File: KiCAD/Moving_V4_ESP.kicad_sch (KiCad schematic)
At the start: 59 parts, among them J1 Vin_1, J2 Vin_2, J3 Power_SW, J4 USB_B_Micro, J5 MOTOR_R, J6 Motor_L, Q1 U4_ALT2, Q2 U4_ALT2, Q3 U4_ALT2, SW1 SW_Reset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

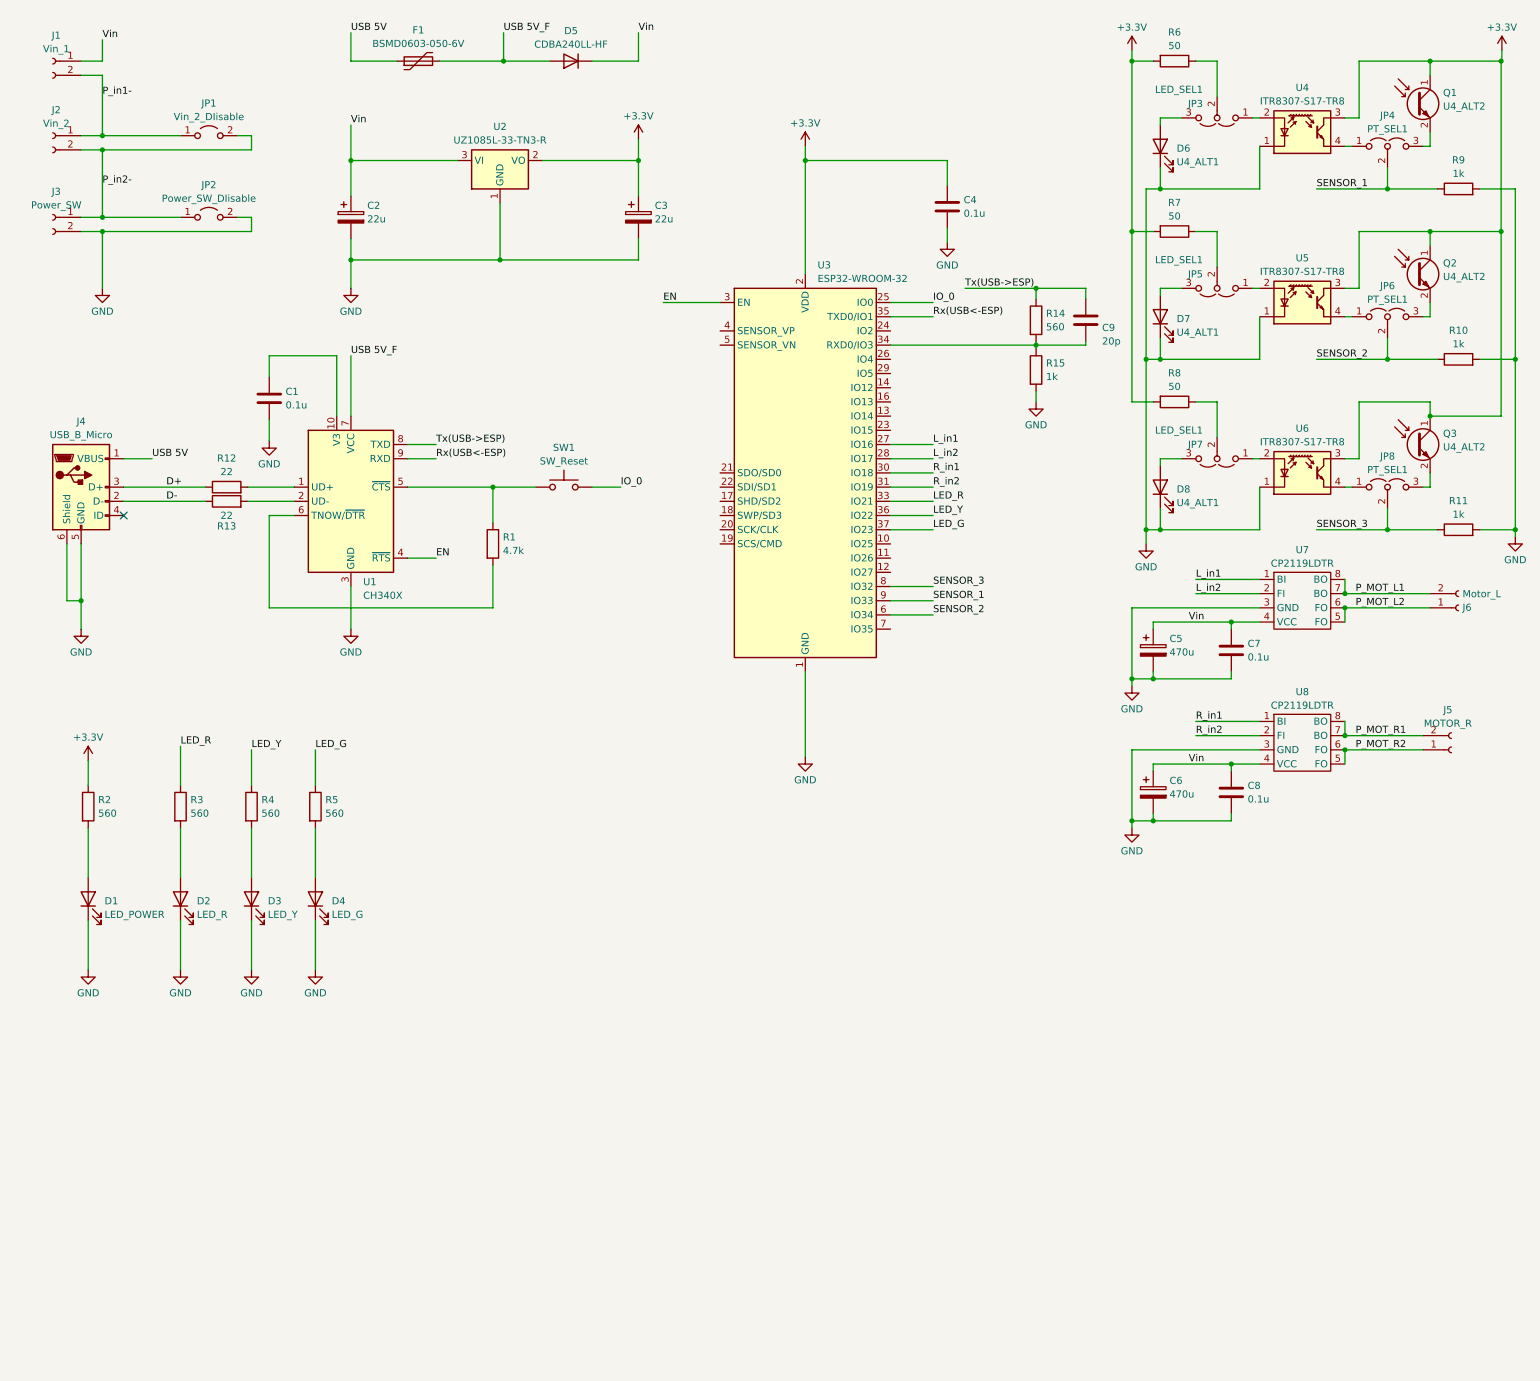
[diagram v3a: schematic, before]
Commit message: 機能ピンのプルアップ・プルダウンを追加
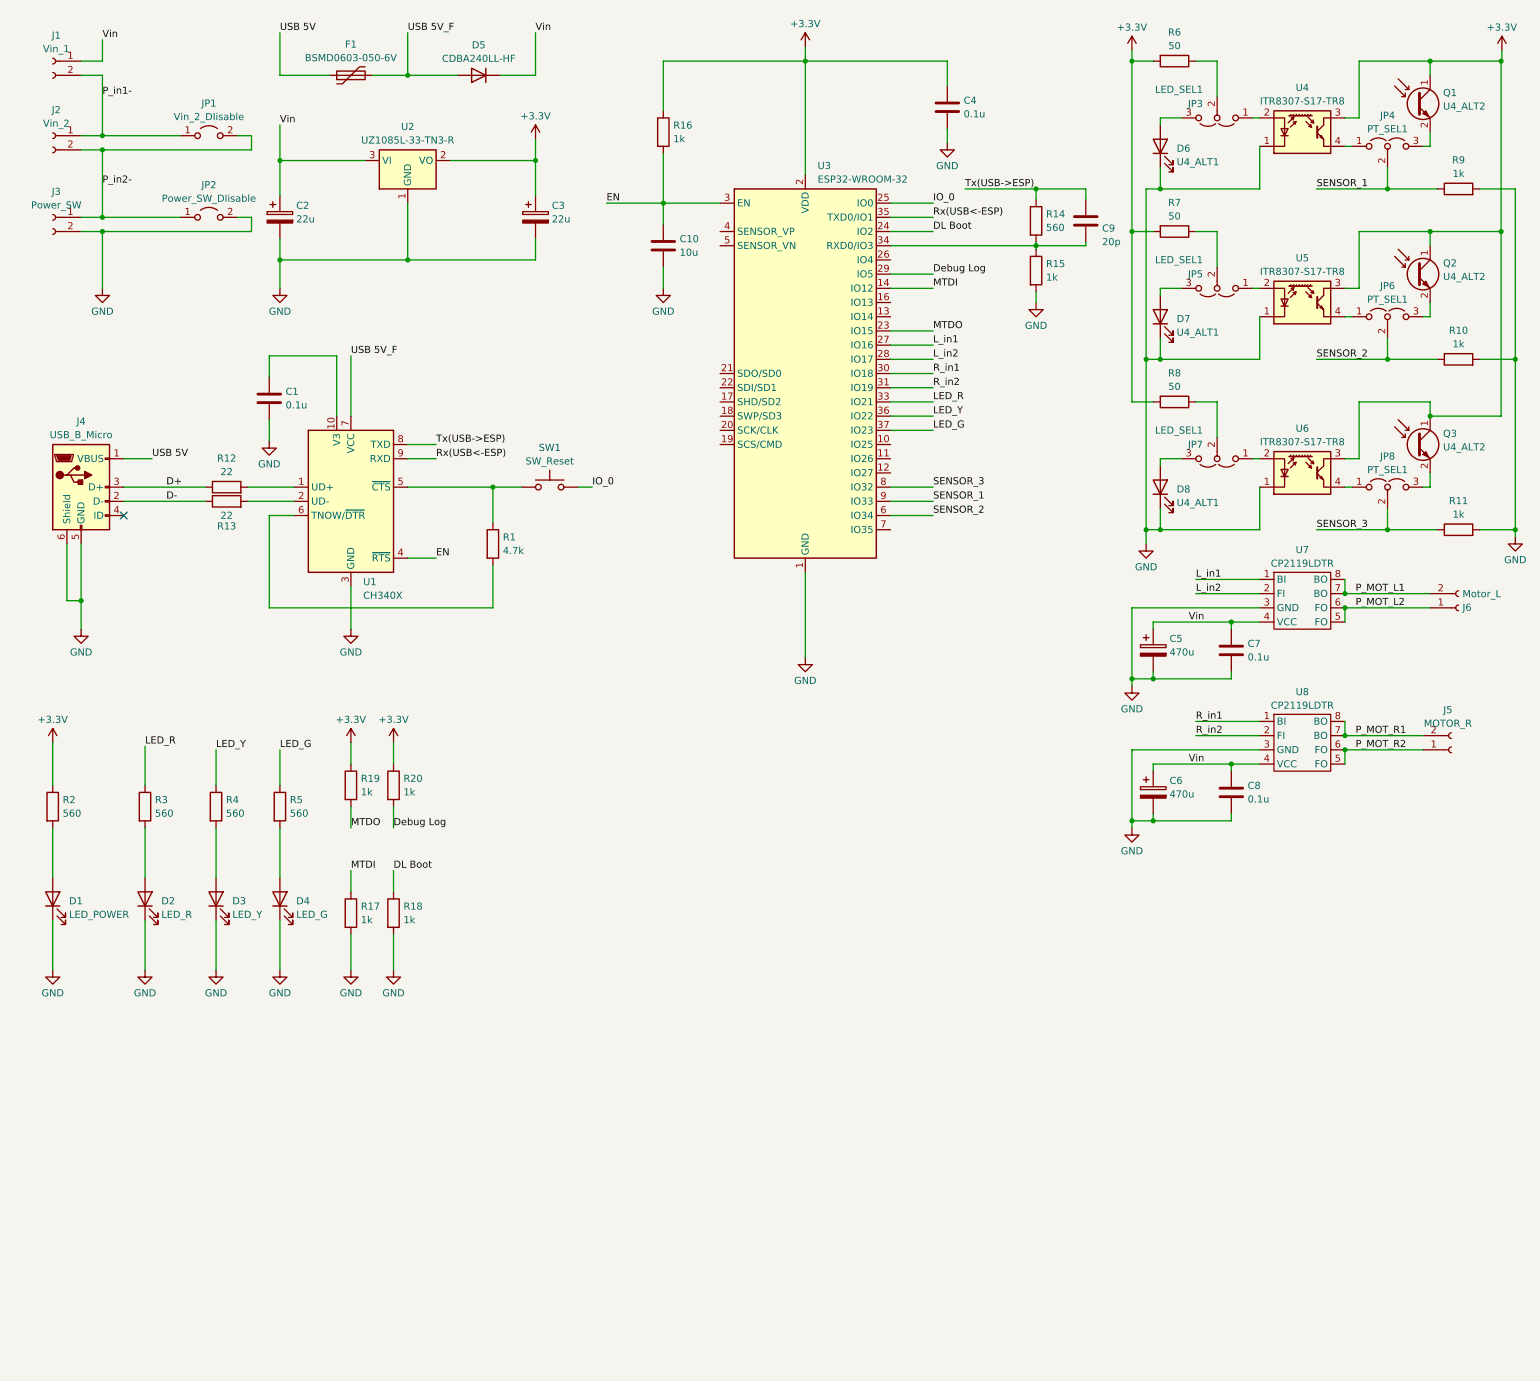
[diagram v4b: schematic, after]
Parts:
- added C10: 10u, Capacitor_SMD:C_0402_1005Metric, symbol Device:C
- added R16, R17, R18, R19, R20: 1k, Resistor_SMD:R_0402_1005Metric, symbol Device:R
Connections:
- net +3.3V: now also R16.1, R19.1, R20.1
- net EN: now also C10.1, R16.2
- net GND: now also C10.2, R17.2, R18.2
- net MTDI: now reaches U3.14 (IO12)
- net MTDI: now also R17.1
- net MTDO: now reaches U3.23 (IO15)
- net MTDO: now also R19.2
- net DL Boot: now reaches U3.24 (IO2)
- net DL Boot: now also R18.1
- net Debug Log: now reaches U3.29 (IO5)
- net Debug Log: now also R20.2
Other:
- moved on the sheet: C2, C3, C4, C9, D1, D2, D3, D4, D5, F1, R14, R15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

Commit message: 5Vの系列を追加
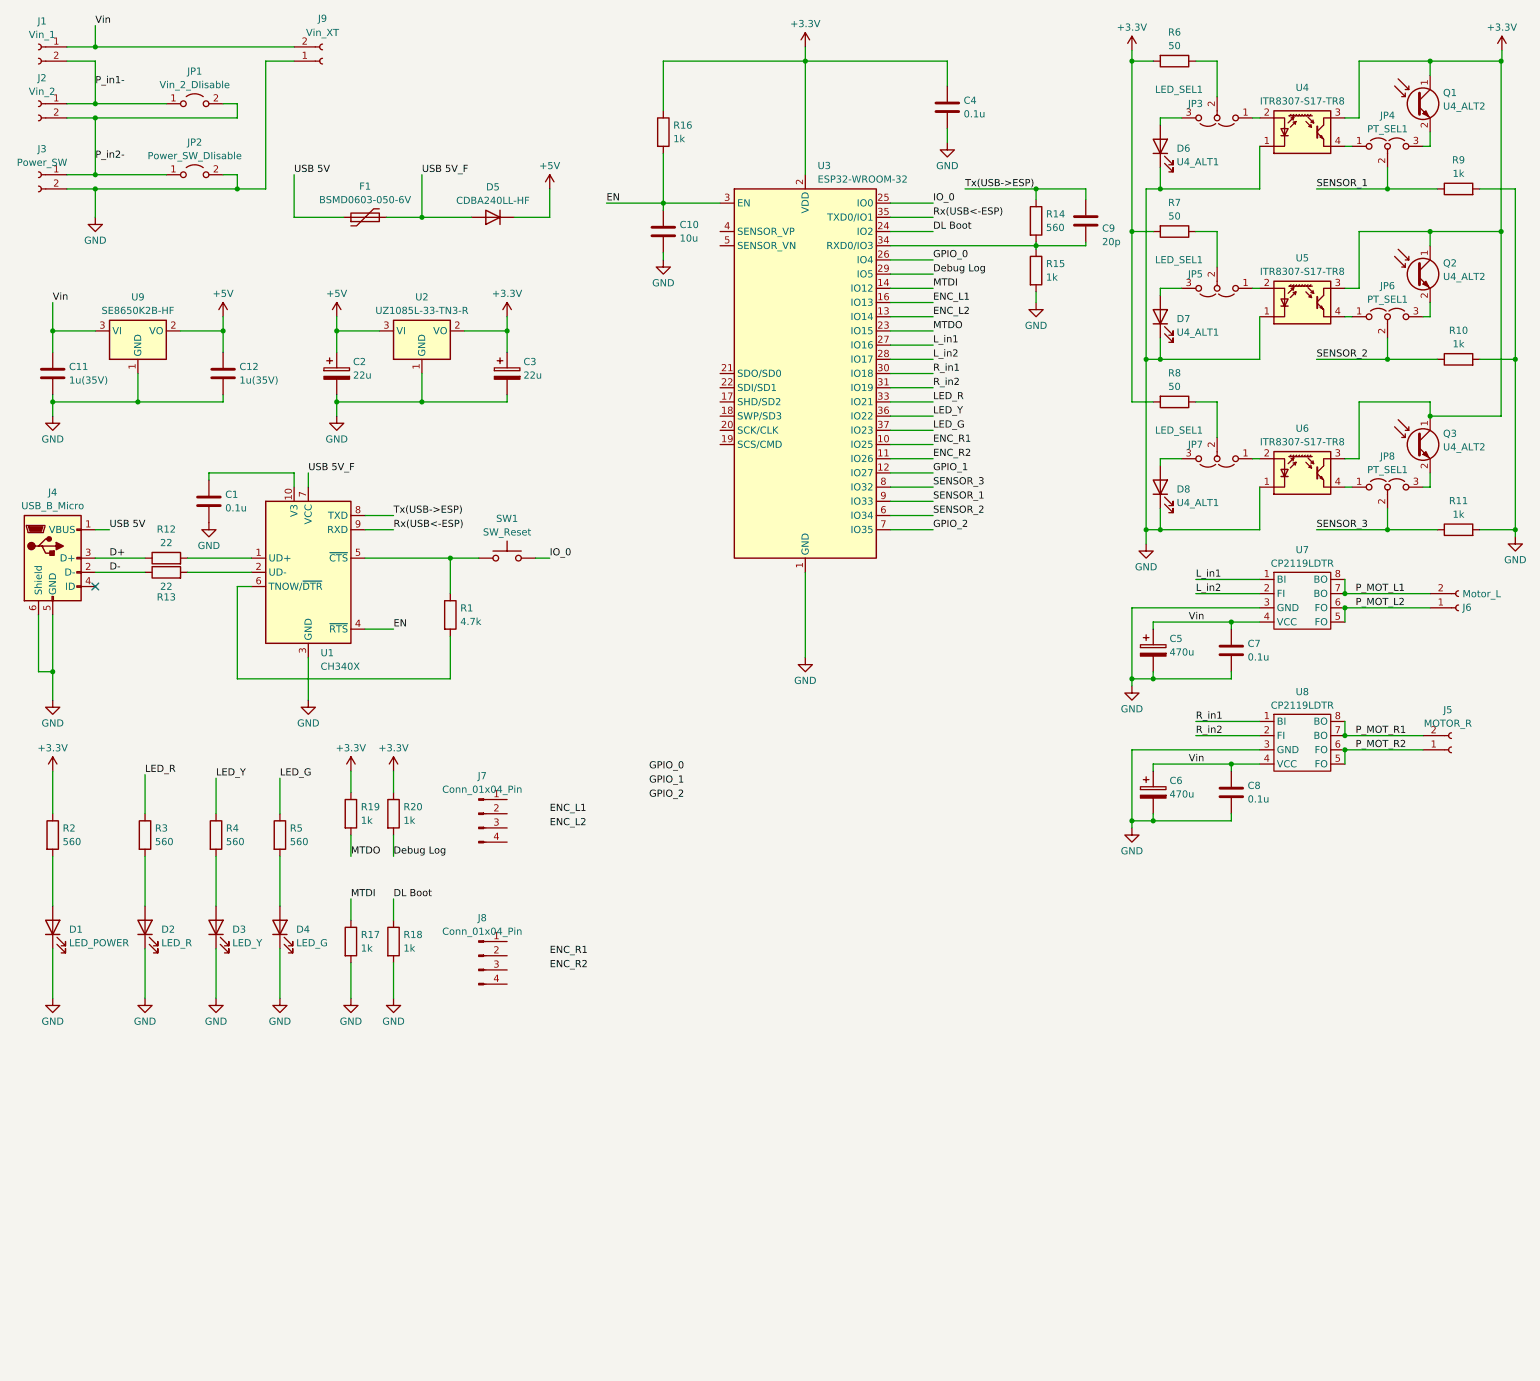
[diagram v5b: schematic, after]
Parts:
- added C11, C12: 1u(35V), Capacitor_SMD:C_0402_1005Metric, symbol Device:C
- added J7, J8: Conn_01x04_Pin, symbol Connector:Conn_01x04_Pin
- added J9: Vin_XT, Connector_AMASS:AMASS_XT60-M_1x02_P7.20mm_Vertical, symbol Connector:Conn_01x02_Socket
- added U9: SE8650K2B-HF, Package_TO_SOT_SMD:SOT-89-3, symbol Regulator_Linear:AP1117-33
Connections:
- net GND: now also C11.2, C12.2, J9.1 (Pin_1), U9.1 (GND)
- net Vin: now also C11.1, J9.2 (Pin_2), U9.3 (VI); no longer C2.1, D5.1 (K), U2.3 (VI)
- net ENC_R1: now reaches U3.10 (IO25)
- net ENC_R2: now reaches U3.11 (IO26)
- net GPIO_1: now reaches U3.12 (IO27)
- net ENC_L2: now reaches U3.13 (IO14)
- net ENC_L1: now reaches U3.16 (IO13)
- net GPIO_0: now reaches U3.26 (IO4)
- net GPIO_2: now reaches U3.7 (IO35)
- new net +5V: C12.1, C2.1, D5.1 (K), U2.3 (VI), U9.2 (VO)
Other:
- moved on the sheet: C1, C10, C2, C3, D1, D2, D3, D4, D5, F1, J1, J2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

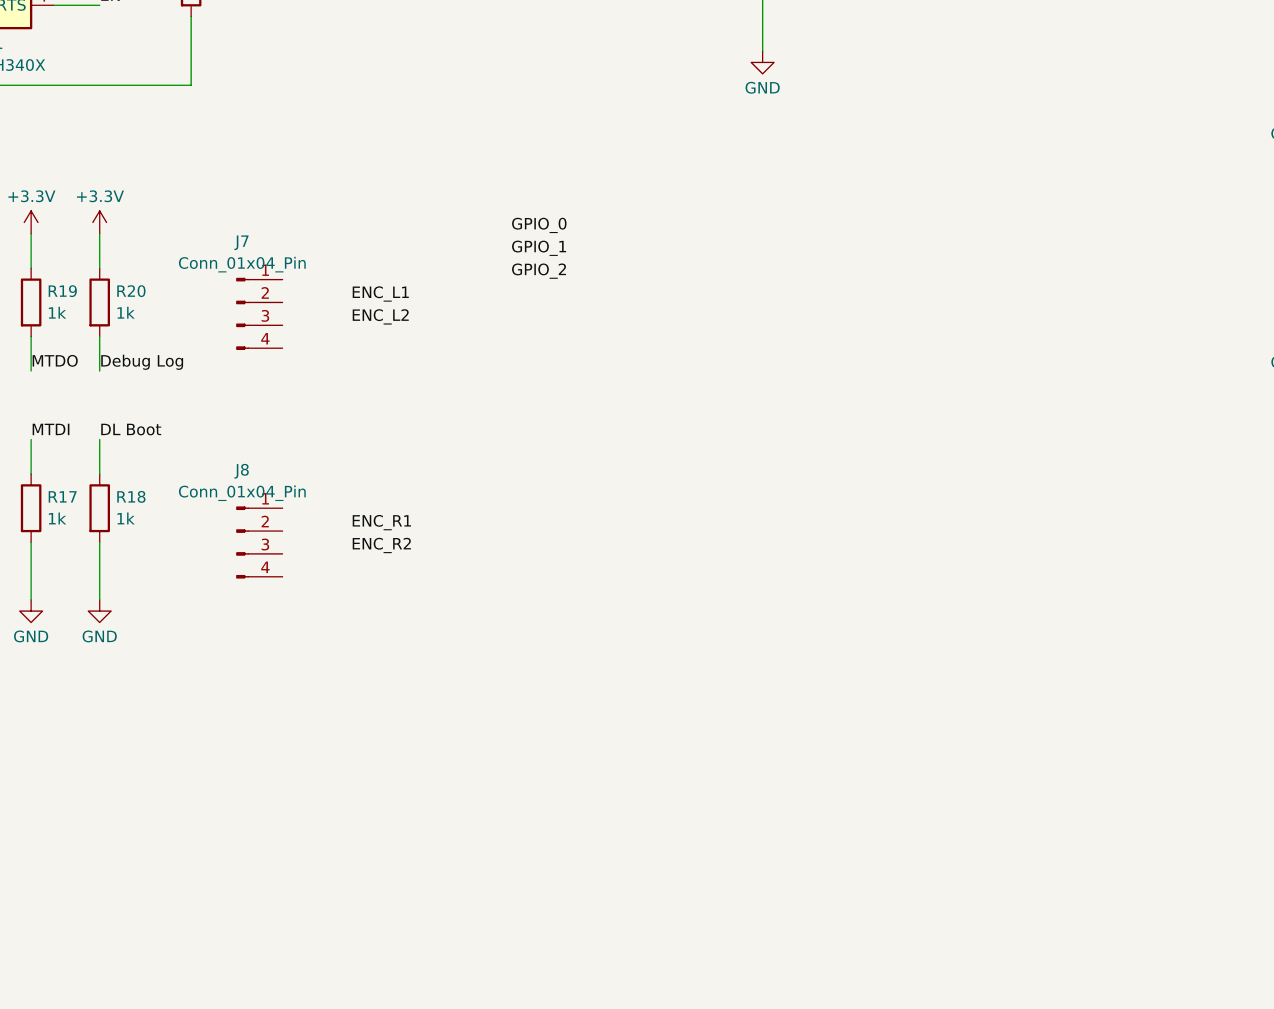
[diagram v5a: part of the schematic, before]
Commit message: エンコーダ回路を追加(仮、要レベルコンバータ)
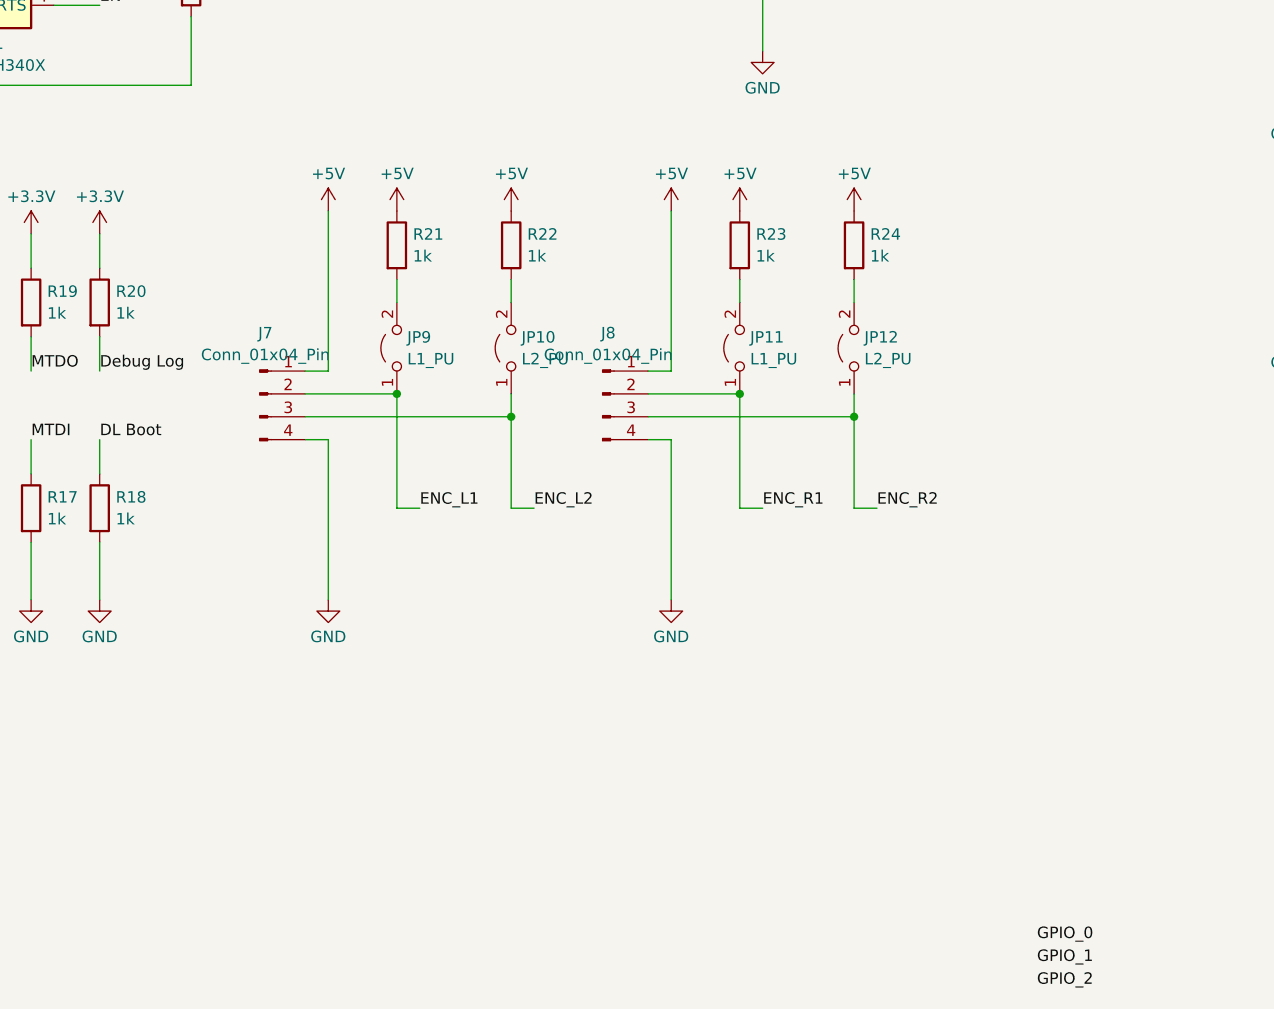
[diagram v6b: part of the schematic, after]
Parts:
- added JP10, JP12: L2_PU, Jumper:SolderJumper-2_P1.3mm_Open_RoundedPad1.0x1.5mm, symbol Jumper:Jumper_2_Open
- added JP11, JP9: L1_PU, Jumper:SolderJumper-2_P1.3mm_Open_RoundedPad1.0x1.5mm, symbol Jumper:Jumper_2_Open
- added R21, R22, R23, R24: 1k, Resistor_SMD:R_0402_1005Metric, symbol Device:R
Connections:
- net +5V: now also J7.1 (Pin_1), J8.1 (Pin_1), R21.1, R22.1, R23.1, R24.1
- net ENC_L1: now also J7.2 (Pin_2), JP9.1 (A)
- net ENC_L2: now also J7.3 (Pin_3), JP10.1 (A)
- net ENC_R1: now also J8.2 (Pin_2), JP11.1 (A)
- net ENC_R2: now also J8.3 (Pin_3), JP12.1 (A)
- net GND: now also J7.4 (Pin_4), J8.4 (Pin_4)
- new net: JP10.2 (B), R22.2
- new net: JP11.2 (B), R23.2
- new net: JP12.2 (B), R24.2
- new net: JP9.2 (B), R21.2
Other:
- moved on the sheet: J7, J8
